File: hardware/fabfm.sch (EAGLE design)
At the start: 36 parts, among them J1 POWER_JACKPTH_LOCK, J2 AVR_SPI_PRG_6PTH, U1 LM386, U2 Encoder, U5 V_REG_317SINK

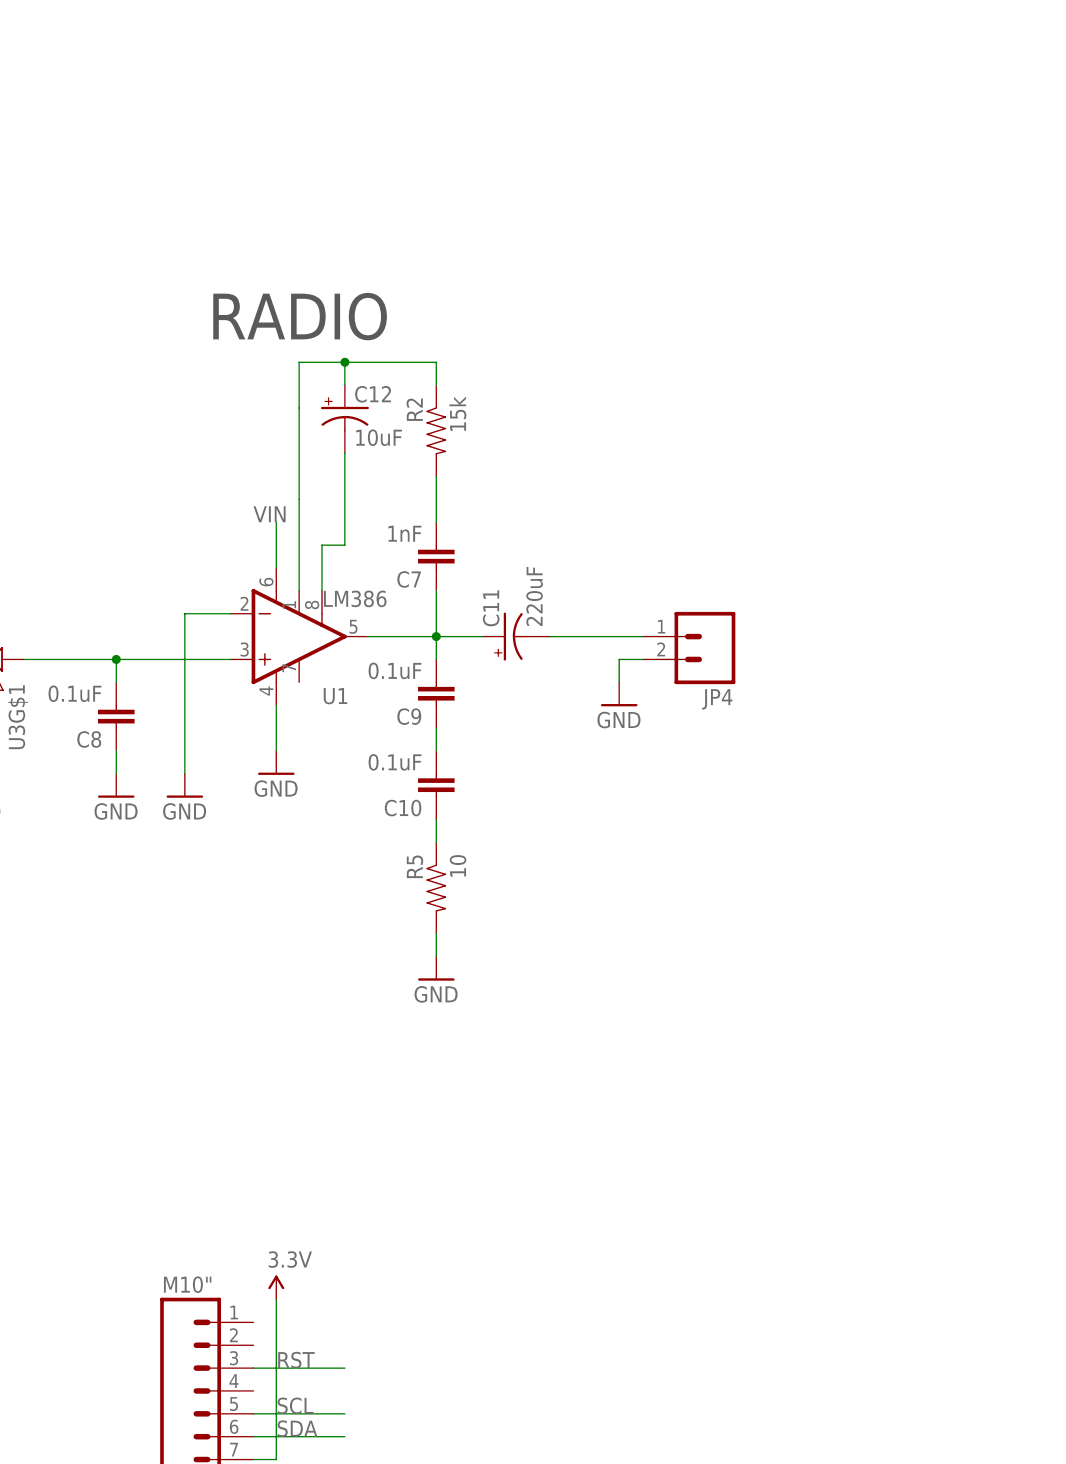
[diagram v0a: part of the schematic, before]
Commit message: v11
-fixed silk mistake
-added locking FP for radio module
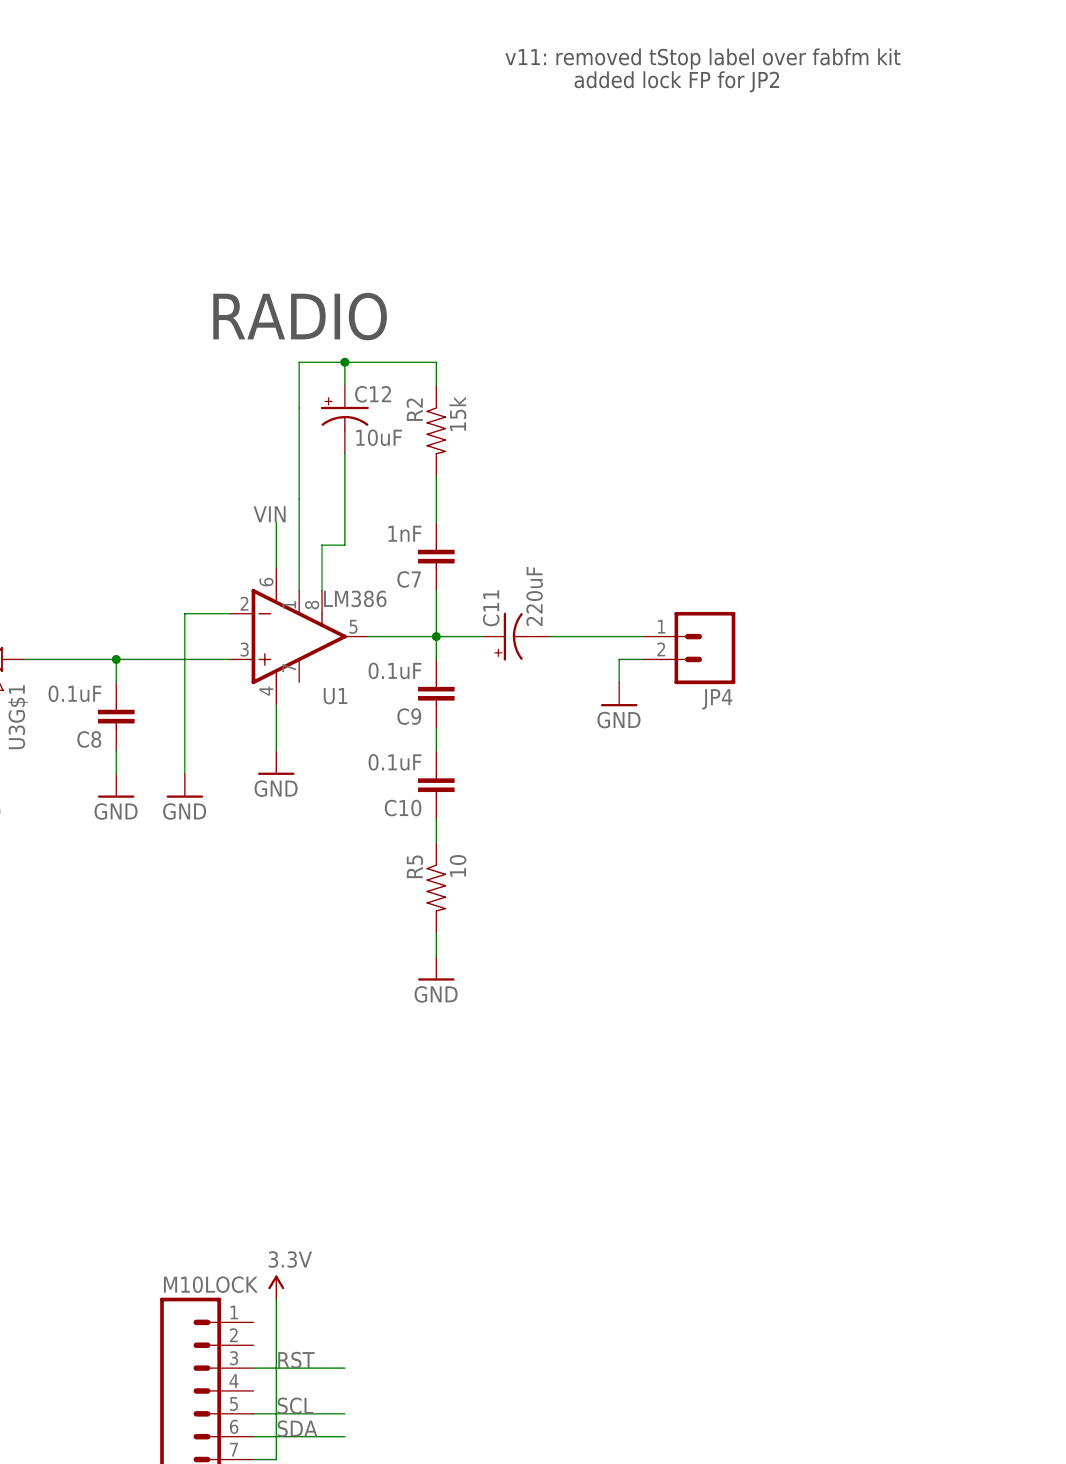
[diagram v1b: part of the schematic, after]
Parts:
- JP2: value M10" -> M10LOCK; device SparkFun-Connectors:M10" -> SparkFun-Connectors:M10LOCK
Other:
- note added: "added lock FP for JP2"
- note added: "v11: removed tStop label over fabfm kit"
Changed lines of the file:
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@@
 <?xml version="1.0" encoding="utf-8"?>
 <!DOCTYPE eagle SYSTEM "eagle.dtd">
-<eagle version="6.2">
+<eagle version="6.3">
 <drawing>
 <settings>
@@
 <part name="SJ1" library="SparkFun-Passives" deviceset="SOLDERJUMPER" device="NO"/>
 <part name="JP9" library="SparkFun" deviceset="LOGO-SFE" device="NEW"/>
-<part name="JP2" library="SparkFun-Connectors" deviceset="M10" device="&quot;"/>
+<part name="JP2" library="SparkFun-Connectors" deviceset="M10" device="LOCK" value="M10LOCK"/>
 <part name="JP12" library="SparkFun-Connectors" deviceset="M07" device=""/>
 <part name="GND17" library="SparkFun" deviceset="GND" device=""/>
@@
 <text x="165.1" y="88.9" size="1.778" layer="97">*internal pullups enabled*</text>
 <text x="45.72" y="180.34" size="1.778" layer="97">*it is suggested to use a 9V wall wart with at least 100mA output</text>
+<text x="322.58" y="251.46" size="1.778" layer="97">v11: removed tStop label over fabfm kit</text>
+<text x="330.2" y="248.92" size="1.778" layer="97">added lock FP for JP2</text>
 </plain>
 <instances>
